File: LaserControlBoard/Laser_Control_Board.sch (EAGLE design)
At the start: 36 parts, among them J1 Servo Header, J2 FTDI Header, J5 FEMALE 2x3, J6 455-1750-1-ND, U1 ATMEGA328P_TQFP, Y1 16MHz

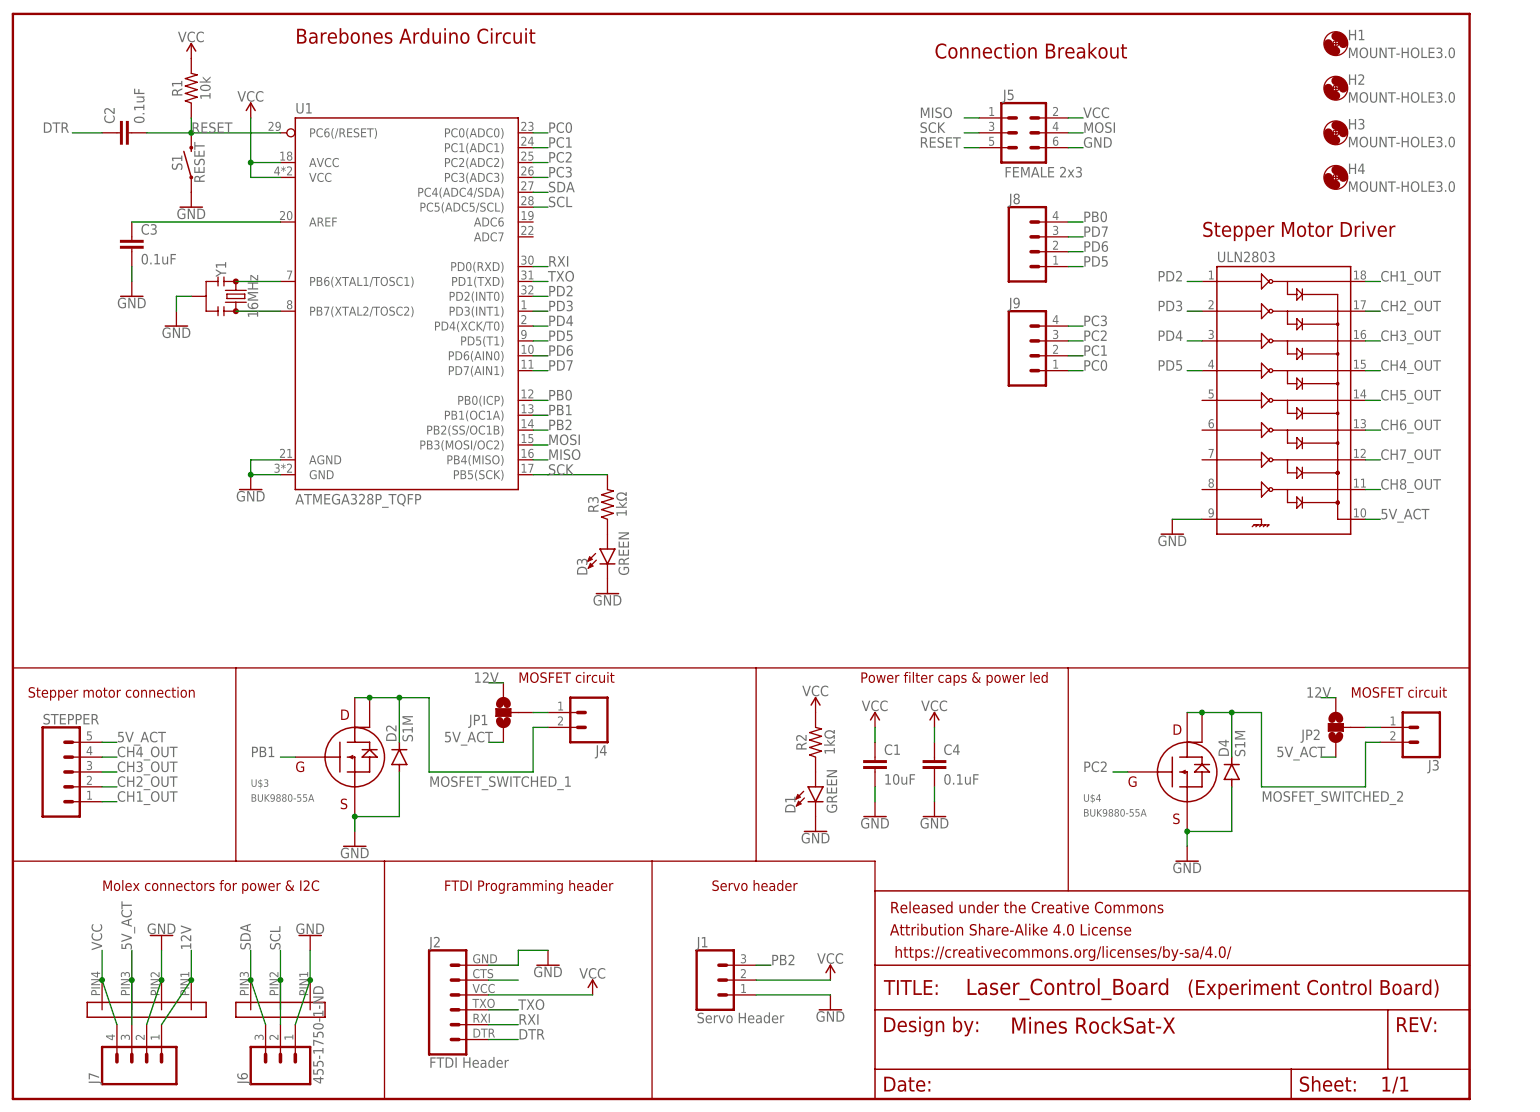
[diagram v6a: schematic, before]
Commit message: Lots of Labels added, GND connections added, component labels embiggened, traces rerouted.
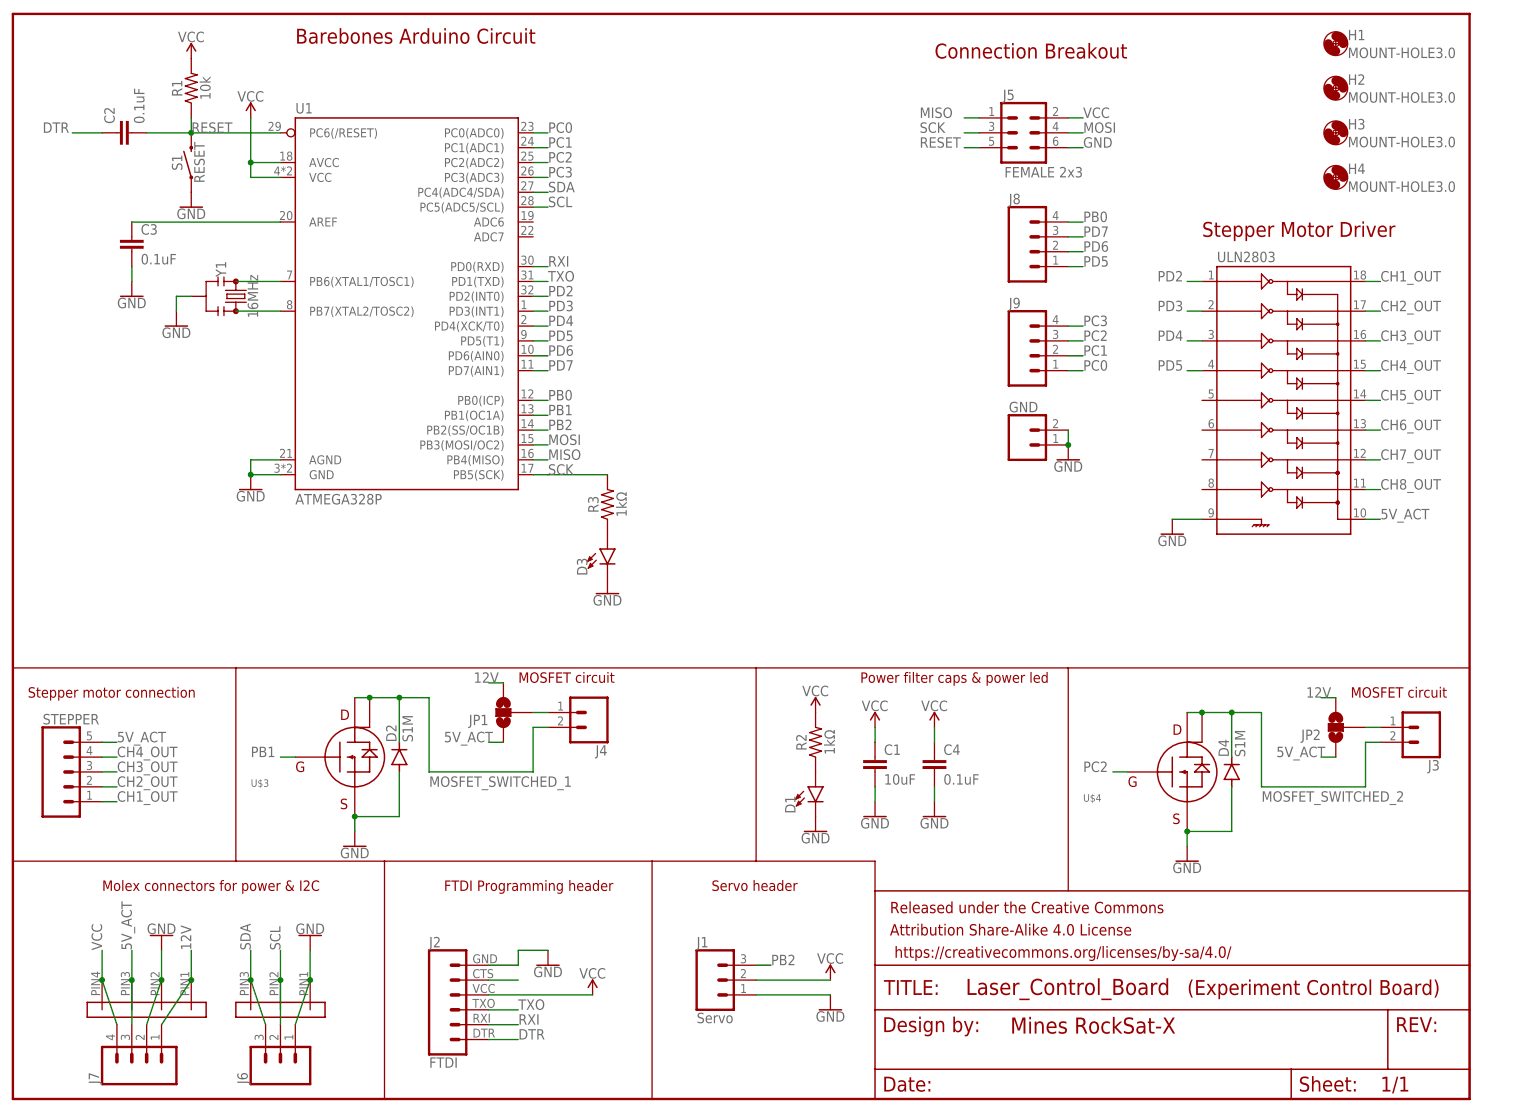
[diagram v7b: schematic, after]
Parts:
- added GND: (no value), SparkFun-Connectors:CONN_02LOCK_LONGPADS
- D1, D3: value GREEN -> (none)
- J1: value Servo Header -> Servo
- J2: value FTDI Header -> FTDI
- J6: value 455-1750-1-ND -> (none)
- U1: value ATMEGA328P_TQFP -> ATMEGA328P
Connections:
- net GND: now also GND.1, GND.2
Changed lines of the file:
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@@
 </classes>
 <parts>
-<part name="U1" library="SparkFun-IC-Microcontroller" deviceset="ATMEGA328P_TQFP" device="" value="ATMEGA328P_TQFP"/>
-<part name="J1" library="SparkFun-Connectors" deviceset="CONN_03" device="" value="Servo Header"/>
-<part name="J2" library="SparkFun-Connectors" deviceset="6_PIN_SERIAL_CABLE" device="PTH" value="FTDI Header"/>
+<part name="U1" library="SparkFun-IC-Microcontroller" deviceset="ATMEGA328P_TQFP" device="" value="ATMEGA328P"/>
+<part name="J1" library="SparkFun-Connectors" deviceset="CONN_03" device="" value="Servo"/>
+<part name="J2" library="SparkFun-Connectors" deviceset="6_PIN_SERIAL_CABLE" device="PTH" value="FTDI"/>
 <part name="ULN2803" library="SparkFun-IC-Special-Function" deviceset="ULN2803" device="SOICW"/>
 <part name="C1" library="SparkFun-Capacitors" deviceset="10UF" device="-0805-10V-10%" value="10uF"/>
@@
 <part name="GND13" library="SparkFun-PowerSymbols" deviceset="GND" device=""/>
 <part name="D2" library="diode" library_urn="urn:adsk.eagle:library:210" deviceset="S1M" device="" package3d_urn="urn:adsk.eagle:package:43460/3"/>
-<part name="D1" library="SparkFun-LED" deviceset="LED-GREEN" device="1206" value="GREEN"/>
-<part name="U$3" library="PowerManagementParts" deviceset="BUK9880-55A" device="" package3d_urn="urn:adsk.eagle:package:43439/1"/>
+<part name="D1" library="SparkFun-LED" deviceset="LED-GREEN" device="1206"/>
+<part name="U$3" library="PowerManagementParts" deviceset="BUK9880-55A" device="" package3d_urn="urn:adsk.eagle:package:43439/1" value=""/>
 <part name="J4" library="SparkFun-Connectors" deviceset="CONN_02" device=""/>
 <part name="GND1" library="SparkFun-PowerSymbols" deviceset="GND" device=""/>
 <part name="R3" library="SparkFun-Resistors" deviceset="RESISTOR" device="0805" value="1kΩ"/>
-<part name="D3" library="SparkFun-LED" deviceset="LED-GREEN" device="1206" value="GREEN"/>
+<part name="D3" library="SparkFun-LED" deviceset="LED-GREEN" device="1206"/>
 <part name="GND14" library="SparkFun-PowerSymbols" deviceset="GND" device=""/>
 <part name="JP1" library="SparkFun-Jumpers" deviceset="JUMPER-SMT_3_NO" device="_NO_SILK" value=""/>
 <part name="J5" library="SparkFun-Connectors" deviceset="CONN_03X2" device="FEMALE" value="FEMALE 2x3"/>
 <part name="D4" library="diode" library_urn="urn:adsk.eagle:library:210" deviceset="S1M" device="" package3d_urn="urn:adsk.eagle:package:43460/3"/>
-<part name="U$4" library="PowerManagementParts" deviceset="BUK9880-55A" device="" package3d_urn="urn:adsk.eagle:package:43439/1"/>
+<part name="U$4" library="PowerManagementParts" deviceset="BUK9880-55A" device="" package3d_urn="urn:adsk.eagle:package:43439/1" value=""/>
 <part name="J3" library="SparkFun-Connectors" deviceset="CONN_02" device=""/>
 <part name="GND15" library="SparkFun-PowerSymbols" deviceset="GND" device=""/>
 <part name="JP2" library="SparkFun-Jumpers" deviceset="JUMPER-SMT_3_NO" device="_NO_SILK" value=""/>
-<part name="J6" library="SparkFun-Connectors" deviceset="CONN_03" device="" value="455-1750-1-ND"/>
+<part name="J6" library="SparkFun-Connectors" deviceset="CONN_03" device=""/>
 <part name="J7" library="SparkFun-Connectors" deviceset="CONN_04" device="LOCK"/>
 <part name="J8" library="SparkFun-Connectors" deviceset="CONN_04" device="LOCK"/>
 <part name="J9" library="SparkFun-Connectors" deviceset="CONN_04" device="LOCK"/>
+<part name="GND" library="SparkFun-Connectors" deviceset="CONN_02" device="LOCK_LONGPADS"/>
+<part name="GND16" library="SparkFun-PowerSymbols" deviceset="GND" device=""/>
 </parts>
 <sheets>
@@
 <attribute name="NAME" x="170.18" y="135.128" size="1.778" layer="95" font="vector"/>
 </instance>
+<instance part="GND" gate="G$1" x="172.72" y="111.76" smashed="yes">
+<attribute name="VALUE" x="170.18" y="106.934" size="1.778" layer="96" font="vector"/>
+<attribute name="NAME" x="170.18" y="117.348" size="1.778" layer="95" font="vector"/>
+</instance>
+<instance part="GND16" gate="1" x="180.34" y="109.22" smashed="yes">
+<attribute name="VALUE" x="180.34" y="108.966" size="1.778" layer="96" align="top-center"/>
+</instance>
 </instances>
 <busses>
@@
 <pinref part="GND15" gate="1" pin="GND"/>
 </segment>
+<segment>
+<pinref part="GND" gate="G$1" pin="1"/>
+<pinref part="GND16" gate="1" pin="GND"/>
+<pinref part="GND" gate="G$1" pin="2"/>
+<wire x1="180.34" y1="114.3" x2="180.34" y2="111.76" width="0.1524" layer="91"/>
+<junction x="180.34" y="111.76"/>
+</segment>
 </net>
